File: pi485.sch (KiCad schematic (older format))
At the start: 27 parts, among them J1 RS485, P1 Rasperry Pi, P2 PWR, P3 Term, P4 Latch Disable, Q1 2N4401, Q2 2N4401, Q3 2N4401, U1 NE555, U2 MAX485

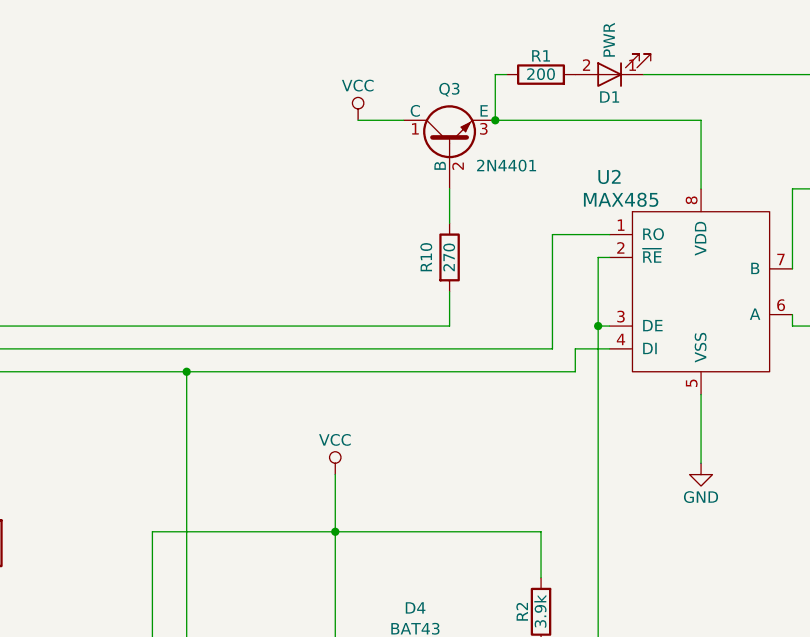
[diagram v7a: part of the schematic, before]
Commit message: VCC control of the 555. Using a GPIO pin, we can reduce overall power consumption by turning things off when we don't need them.
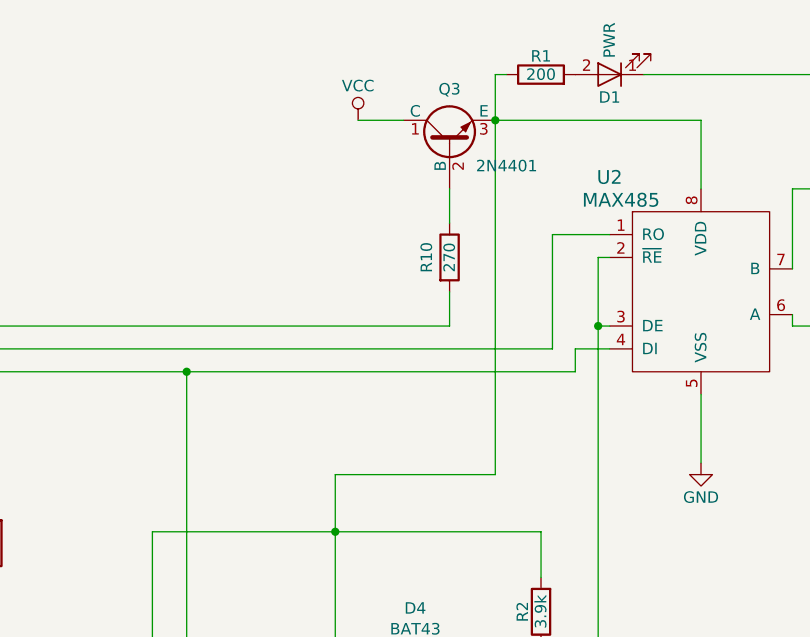
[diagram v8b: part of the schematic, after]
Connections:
- net VCC: no longer R2.2, U1.4 (R), U1.8 (VCC)
- net at Q3.3 (E), R1.1, U2.8 (VDD): now also R2.2, U1.4 (R), U1.8 (VCC)
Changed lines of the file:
@@
-$EndComp
-$Comp
-L VCC #PWR08
-U 1 1 586E9922
-P 5500 3550
-F 0 "#PWR08" H 5500 3400 50  0001 C CNN
-F 1 "VCC" H 5500 3700 50  0000 C CNN
-F 2 "" H 5500 3550 50  0000 C CNN
-F 3 "" H 5500 3550 50  0000 C CNN
-	1    5500 3550
-	1    0    0    -1
 $EndComp
 $Comp
@@
 	6250 1800 6200 1800
 Wire Wire Line
-	6200 1800 6200 2000
+	6200 1800 6200 3550
 Wire Wire Line
 	6850 1800 8250 1800
@@
 	8250 1800 8250 1900
 Connection ~ 6200 2000
+Wire Wire Line
+	6200 3550 5500 3550
 $EndSCHEMATC
